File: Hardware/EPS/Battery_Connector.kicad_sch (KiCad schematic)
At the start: 1 part

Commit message: Fuse, Power Switch to 3.3V, connector ESD Prot.
v0.0.2
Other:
- title: (none) -> EPS Schematics
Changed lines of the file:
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@@
 (kicad_sch (version 20211123) (generator eeschema)
   (paper "A4")
+  (title_block
+    (title "EPS Schematics")
+    (date "2023-04-08")
+    (rev "v0.0.2")
+    (comment 1 "e-mail: carmamo.95@gmail.com")
+    (comment 2 "Author: Carlos Martinez Mora")
+  )
   (hierarchical_label "VBAT" (shape bidirectional) (at 148.59 67.31 90)
     (effects (font (size 1.27 1.27)) (justify left))

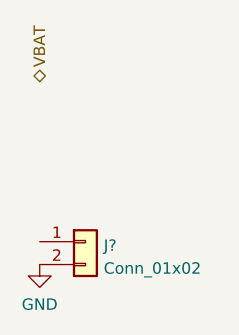
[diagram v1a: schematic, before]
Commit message: Defined pinout for board connector, major revision
v0.0.3 - Fixed erratas and cleaned the schematic
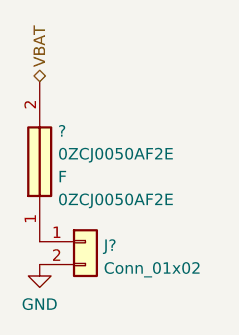
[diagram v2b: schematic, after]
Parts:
- added ?: 0ZCJ0050AF2E, symbol 0ZCJ0050AF2E:0ZCJ0050AF2E
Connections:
- net VBAT: now also ?.2
- net at J?.1 (Pin_1): now also ?.1
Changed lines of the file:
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@@
     (title "EPS Schematics")
     (date "2023-04-08")
-    (rev "v0.0.2")
-    (comment 1 "e-mail: carmamo.95@gmail.com")
+    (rev "v0.0.3")
+    (comment 1 "e-mail: ")
     (comment 2 "Author: Carlos Martinez Mora")
   )
@@
     (effects (font (size 1.27 1.27)) (justify left))
   )
+  (symbol (lib_id "0ZCJ0050AF2E:0ZCJ0050AF2E") (at 148.59 85.09 90) (unit 1)
+    (in_bom yes) (on_board yes) (fields_autoplaced)
+    (property "Reference" "?" (id 0) (at 150.622 72.8284 90)
+      (effects (font (size 1.27 1.27)) (justify right))
+    )
+    (property "Value" "0ZCJ0050AF2E" (id 1) (at 150.622 75.3653 90)
+      (effects (font (size 1.27 1.27)) (justify right))
+    )
+    (property "Footprint" "" (id 2) (at 148.59 85.09 0)
+      (effects (font (size 1.27 1.27)) hide)
+    )
+    (property "Datasheet" "" (id 3) (at 148.59 85.09 0)
+      (effects (font (size 1.27 1.27)) hide)
+    )
+    (property "Reference_1" "F" (id 4) (at 150.622 77.9022 90)
+      (effects (font (size 1.27 1.27)) (justify right))
+    )
+    (property "Value_1" "0ZCJ0050AF2E" (id 5) (at 150.622 80.4391 90)
+      (effects (font (size 1.27 1.27)) (justify right))
+    )
+    (property "Footprint_1" "FUSC3216X120N" (id 6) (at 244.78 71.12 0)
+      (effects (font (size 1.27 1.27)) (justify left top) hide)
+    )
+    (property "Datasheet_1" "https://datasheet.datasheetarchive.com/originals/distributors/Datasheets_SAMA/7d7191d77363ec710a142f55990dd75c.pdf" (id 7) (at 344.78 71.12 0)
+      (effects (font (size 1.27 1.27)) (justify left top) hide)
+    )
+    (property "Height" "1.2" (id 8) (at 544.78 71.12 0)
+      (effects (font (size 1.27 1.27)) (justify left top) hide)
+    )
+    (property "Manufacturer_Name" "BelFuse" (id 9) (at 644.78 71.12 0)
+      (effects (font (size 1.27 1.27)) (justify left top) hide)
+    )
+    (property "Manufacturer_Part_Number" "0ZCJ0050AF2E" (id 10) (at 744.78 71.12 0)
+      (effects (font (size 1.27 1.27)) (justify left top) hide)
+    )
+    (property "Mouser Part Number" "530-0ZCJ0050AF2E" (id 11) (at 844.78 71.12 0)
+      (effects (font (size 1.27 1.27)) (justify left top) hide)
+    )
+    (property "Mouser Price/Stock" "https://www.mouser.co.uk/ProductDetail/Bel-Fuse/0ZCJ0050AF2E?qs=SRYZG9HaIQ3Oqm1PQp276Q%3D%3D" (id 12) (at 944.78 71.12 0)
+      (effects (font (size 1.27 1.27)) (justify left top) hide)
+    )
+    (property "Arrow Part Number" "0ZCJ0050AF2E" (id 13) (at 1044.78 71.12 0)
+      (effects (font (size 1.27 1.27)) (justify left top) hide)
+    )
+    (property "Arrow Price/Stock" "https://www.arrow.com/en/products/0zcj0050af2e/bel-group" (id 14) (at 1144.78 71.12 0)
+      (effects (font (size 1.27 1.27)) (justify left top) hide)
+    )
+    (pin "1")
+    (pin "2")
+  )
   (symbol (lib_id "Connector_Generic:Conn_01x02") (at 153.67 85.09 0) (unit 1)
